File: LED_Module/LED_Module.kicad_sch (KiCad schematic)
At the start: 19 parts, among them J1 Conn_02x05_Odd_Even, J2 Conn_01x03_Male, SW1 SW_Push, U1 LD1117S33TR_SOT223, U2 STM32F091RCTx

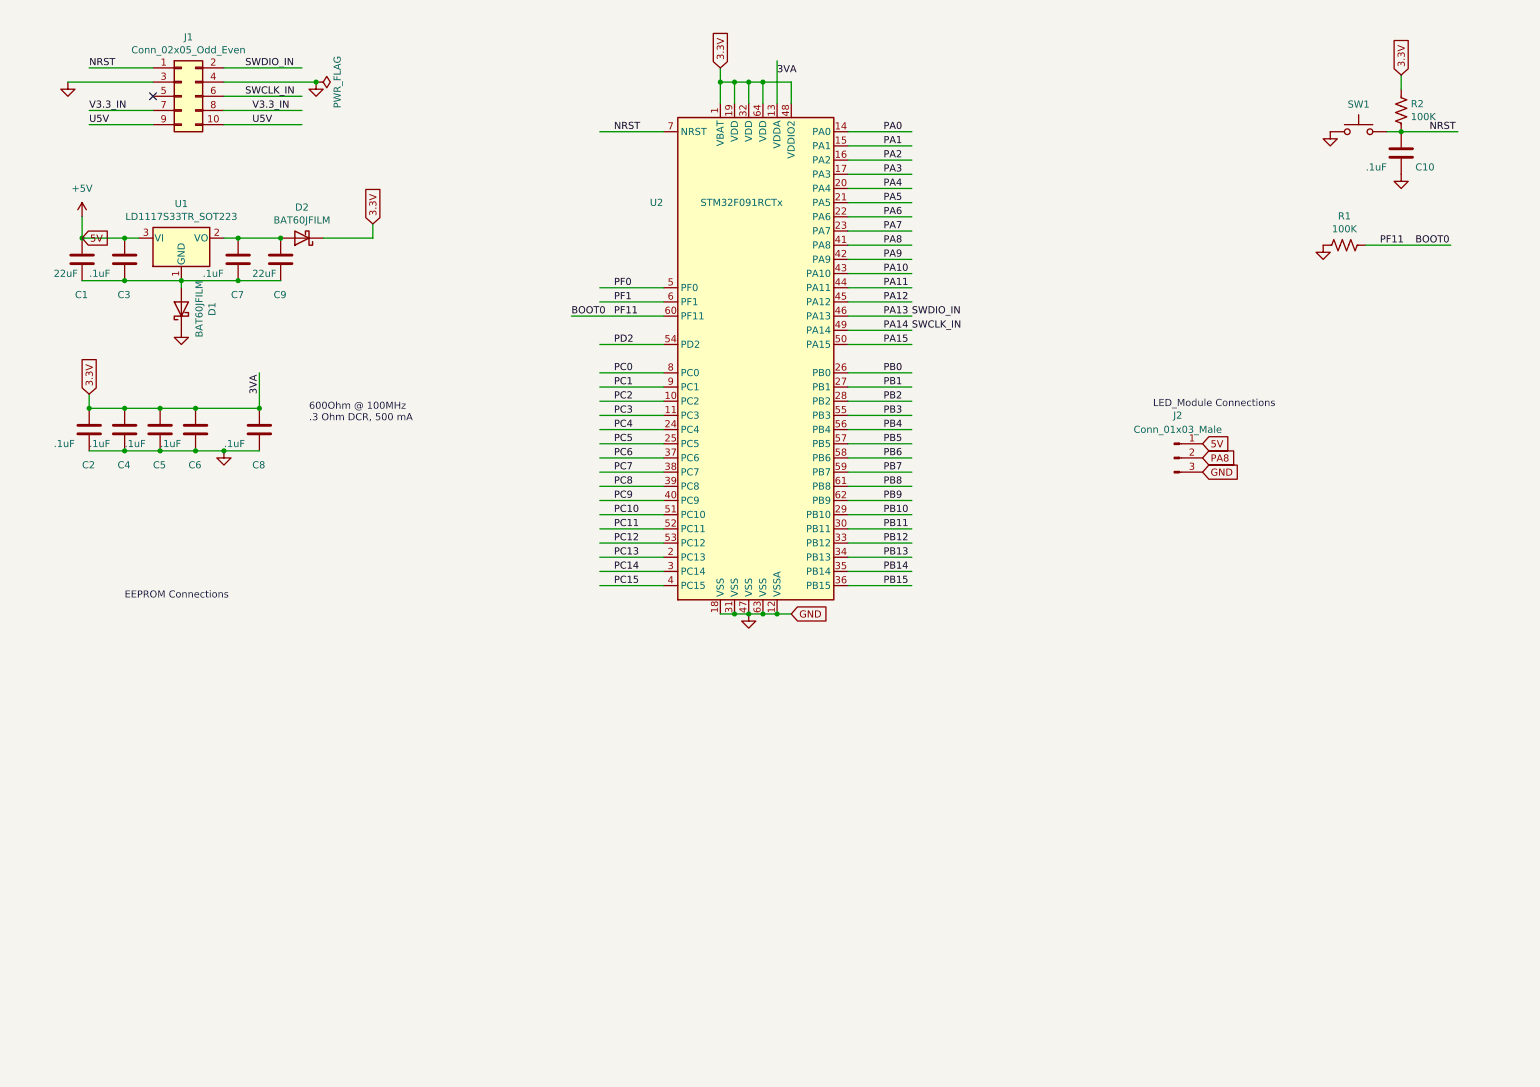
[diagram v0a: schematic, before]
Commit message: Buck Converter and Wifi schematic
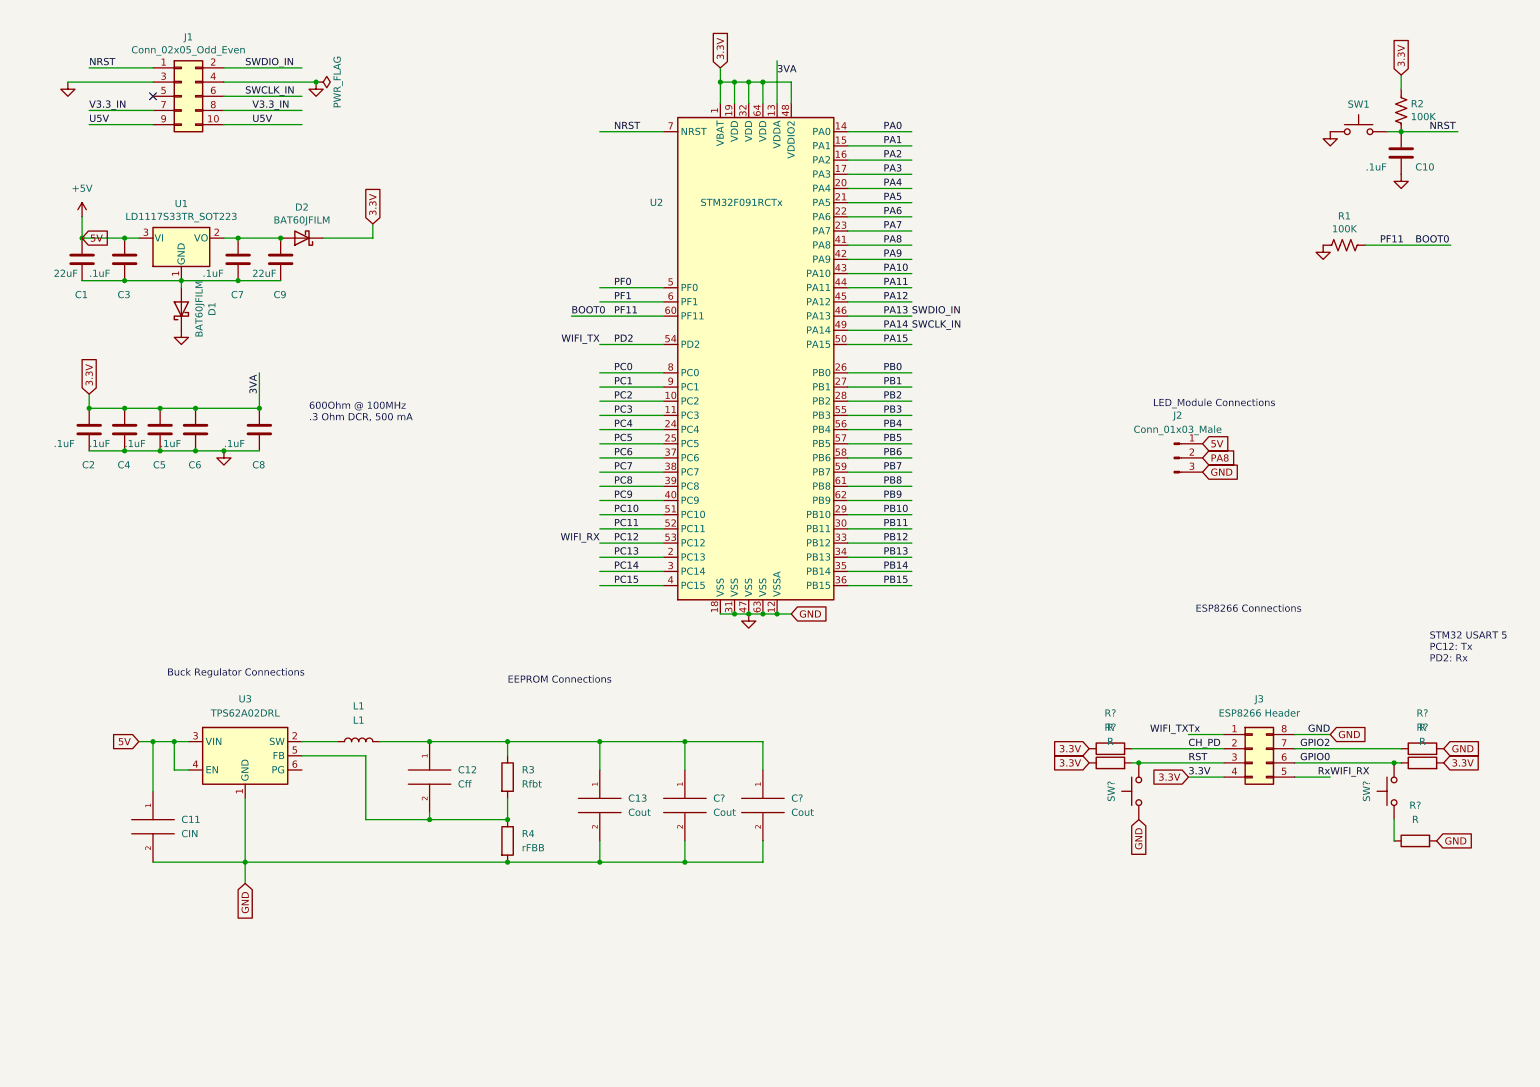
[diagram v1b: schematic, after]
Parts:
- added C11: CIN, Capacitor_SMD:C_0805_2012Metric_Pad1.18x1.45mm_HandSolder, symbol pspice:CAP
- added C12: Cff, Capacitor_SMD:C_0402_1005Metric_Pad0.74x0.62mm_HandSolder, symbol pspice:CAP
- added C13, C? (x2): Cout, Capacitor_SMD:C_0805_2012Metric_Pad1.18x1.45mm_HandSolder, symbol pspice:CAP
- added J3: ESP8266 Header, Connector_PinHeader_2.54mm:PinHeader_2x04_P2.54mm_Vertical, symbol Connector_Generic:Conn_02x04_Counter_Clockwise
- added L1: L1, Inductor_SMD:L_0603_1608Metric_Pad1.05x0.95mm_HandSolder, symbol Device:L
- added R3: Rfbt, Resistor_SMD:R_0805_2012Metric_Pad1.20x1.40mm_HandSolder, symbol Device:R
- added R4: rFBB, Resistor_SMD:R_0805_2012Metric_Pad1.20x1.40mm_HandSolder, symbol Device:R
- added R? (x5): R, symbol Device:R
- added SW? (x2): SW_Push, Button_Switch_SMD:SW_SPST_PTS645, symbol Switch:SW_Push
- added U3: TPS62A02DRL, Package_TO_SOT_SMD:SOT-563, symbol Regulator_Switching:AP62150Z6
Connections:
- net +5V: now also C11.1, U3.3 (VIN), U3.4 (EN)
- net 3.3V: now also J3.4 (3.3V), R?.1, R?.1, R?.2
- net GND: now also C11.2, C13.2, C?.2, C?.2, J3.8 (GND), R4.2, R?.2, R?.2, SW?.1, U3.1 (GND)
- net PC12: now also J3.5 (Rx)
- net PD2: now also J3.1 (Tx)
- new net: L1.1, U3.2 (SW)
- new net: C12.1, C13.1, C?.1, C?.1, L1.2, R3.1
- new net: C12.2, R3.2, R4.1, U3.5 (FB)
- new net: R?.1, SW?.1
- new net CH_PD: J3.2 (CH_PD), R?.2
- new net GPIO0: J3.6 (GPIO0), R?.1, SW?.2
- new net GPIO2: J3.7 (GPIO2), R?.1
- new net RST: J3.3 (RST), R?.2, SW?.2
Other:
- note added: "Buck Regulator Connections"
- note added: "ESP8266 Connections"
- note added: "STM32 USART 5 PC12: Tx PD2: Rx"

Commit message: EEPROM Schematic, Decoupling routing, Buck Layout
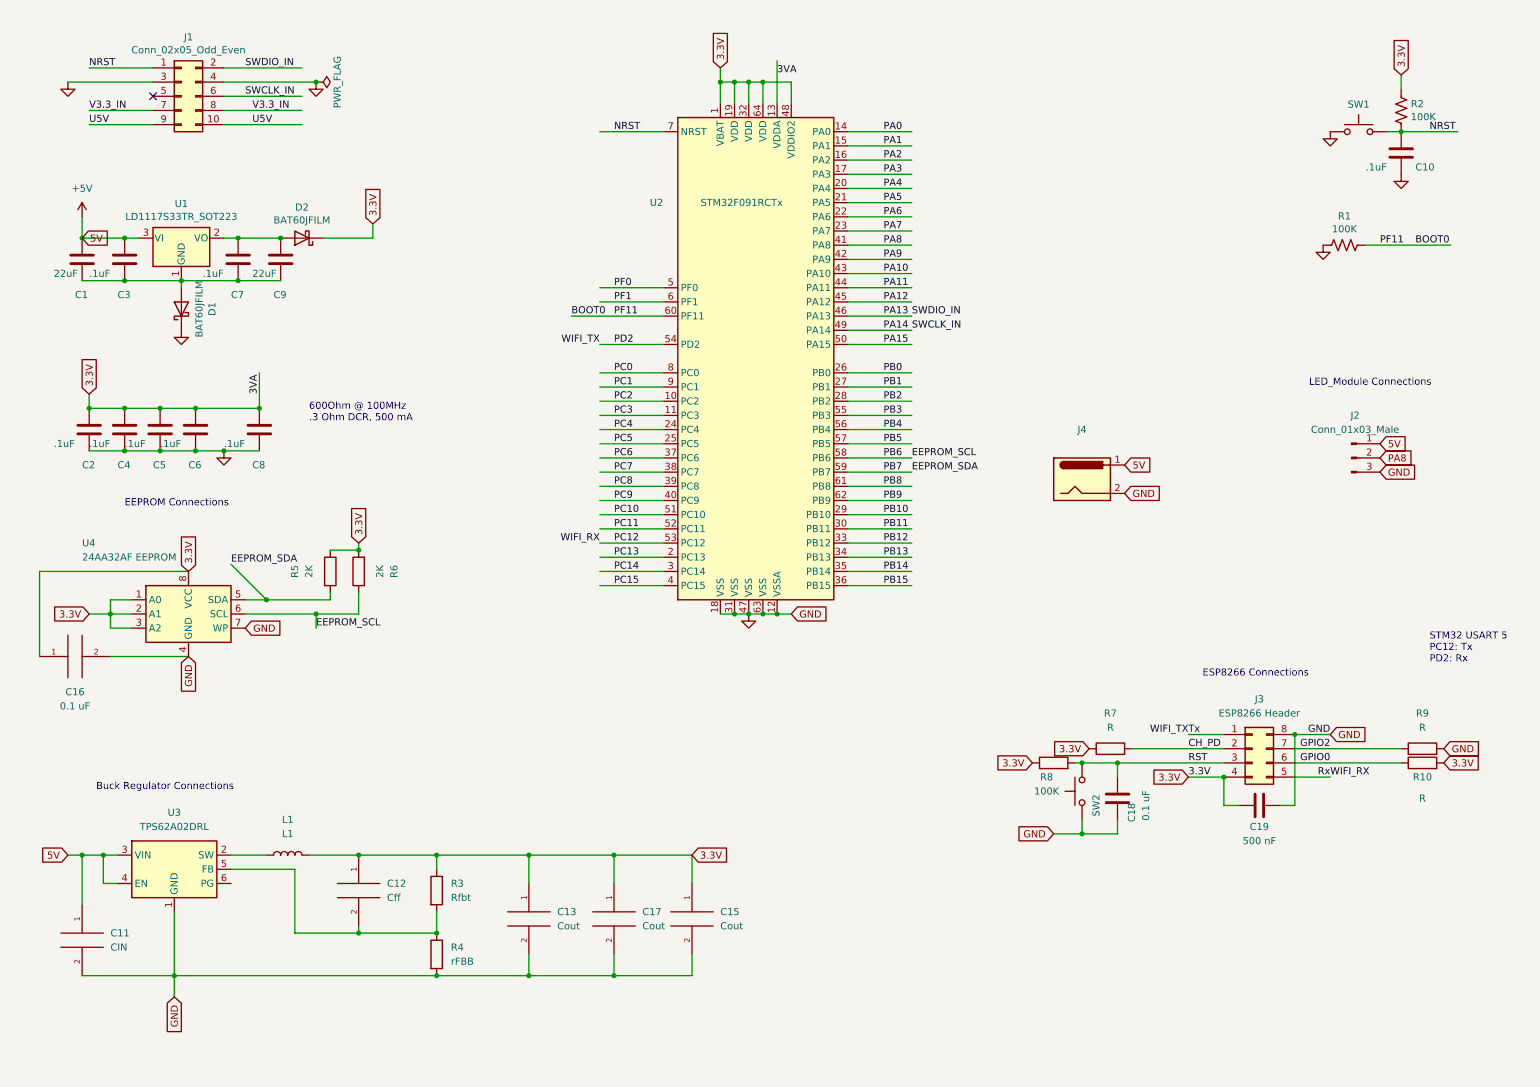
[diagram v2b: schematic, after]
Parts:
- removed C?: Cout, Capacitor_SMD:C_0805_2012Metric_Pad1.18x1.45mm_HandSolder, symbol pspice:CAP
- removed R?: R, symbol Device:R
- removed SW?: SW_Push, Button_Switch_SMD:SW_SPST_PTS645, symbol Switch:SW_Push
- added C16: 0.1 uF, Capacitor_SMD:C_0805_2012Metric_Pad1.18x1.45mm_HandSolder, symbol pspice:CAP
- added C17: Cout, Capacitor_SMD:C_0805_2012Metric_Pad1.18x1.45mm_HandSolder, symbol pspice:CAP
- added C18: 0.1 uF, Capacitor_SMD:C_0805_2012Metric_Pad1.18x1.45mm_HandSolder, symbol Device:C
- added C19: 500 nF, Capacitor_SMD:C_0805_2012Metric_Pad1.18x1.45mm_HandSolder, symbol Device:C
- added J4: (no value), symbol Connector:Barrel_Jack
- added R5, R6: 2K, Resistor_SMD:R_0805_2012Metric_Pad1.20x1.40mm_HandSolder, symbol Device:R
- added U4: 24AA32AF EEPROM, Package_DIP:DIP-8_W7.62mm_Socket, symbol Memory_EEPROM:24LC00
- R10, R7, R9: renamed from R?; footprint (none) -> Resistor_SMD:R_0805_2012Metric_Pad1.20x1.40mm_HandSolder
- R8: renamed from R?; value R -> 100K; footprint (none) -> Resistor_SMD:R_0805_2012Metric_Pad1.20x1.40mm_HandSolder
- gave numbers to parts that had none: 2
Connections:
- net +5V: now also J4.1
- net 3.3V: now also C12.1, C13.1, C15.1, L1.2, R3.1, C16.1, C17.1, C19.2, R5.1, R6.2, U4.1 (A0), U4.2 (A1), U4.3 (A2), U4.8 (VCC)
- net GND: now also C16.2, C17.2, C18.2, C19.1, J4.2, U4.4 (GND), U4.7 (WP)
- net RST: now also C18.1
- net PB6 renamed EEPROM_SCL
- net EEPROM_SCL: now also R6.1, U4.6 (SCL)
- net PB7 renamed EEPROM_SDA
- net EEPROM_SDA: now also R5.2, U4.5 (SDA)
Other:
- moved on the sheet: C11, C12, C13, C15, J2, L1, R3, R4, R8, SW2, U3
